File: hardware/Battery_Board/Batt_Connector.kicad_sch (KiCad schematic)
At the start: 0 parts

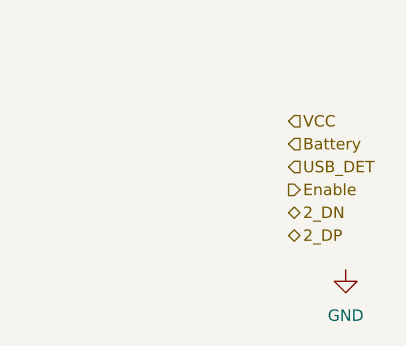
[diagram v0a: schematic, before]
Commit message: feat(Hw):Update_Battery_Sch_And_Sensors_And_PWNCube
pending_Outputs_connectors
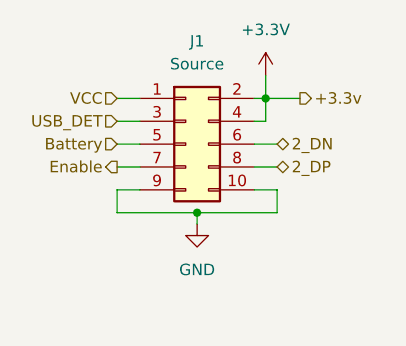
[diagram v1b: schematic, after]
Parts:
- added J1: Source, symbol Connector_Generic:Conn_02x05_Odd_Even
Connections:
- net 2_DN: now also J1.6 (Pin_6)
- net 2_DP: now also J1.8 (Pin_8)
- net Battery: now also J1.5 (Pin_5)
- net Enable: now also J1.7 (Pin_7)
- net GND: now also J1.10 (Pin_10), J1.9 (Pin_9)
- net USB_DET: now also J1.3 (Pin_3)
- net VCC: now also J1.1 (Pin_1)
- new net +3.3V: J1.2 (Pin_2), J1.4 (Pin_4)
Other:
- company: (none) -> Electronic Cats
- title: (none) -> Battery_Board

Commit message: feat(Hw):floorplans_updated
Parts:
- J1: footprint (none) -> Connector_PinHeader_2.54mm:PinHeader_2x05_P2.54mm_Vertical
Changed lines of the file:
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@@
 			)
 		)
-		(property "Footprint" ""
+		(property "Footprint" "Connector_PinHeader_2.54mm:PinHeader_2x05_P2.54mm_Vertical"
 			(at 49.53 54.61 0)
 			(effects

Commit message: feat(Hw):BoM´s_Updated
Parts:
- J1: LCSC# (none) -> C7501191
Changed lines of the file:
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@@
+			)
+		)
+		(property "LCSC#" "C7501191"
+			(at 49.53 54.61 0)
+			(effects
+				(font
+					(size 1.27 1.27)
+				)
+				(hide yes)
 			)
 		)
